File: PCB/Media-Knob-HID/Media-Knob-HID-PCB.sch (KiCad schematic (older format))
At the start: 0 parts

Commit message: Interface und Powersupply
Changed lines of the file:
@@
 $Descr A4 11693 8268
 encoding utf-8
-Sheet 1 5
+Sheet 1 7
 Title "Media-Knob_HID"
-Date "2020-11-08"
+Date "2020-12-13"
 Rev "V0.1"
 Comp "Benedikt Graf"
@@
 $EndDescr
 $Sheet
-S 6400 3400 750  300
+S 7050 3250 750  300
 U 5FAB02B0
 F0 "LED_Ring" 50
 F1 "LED_Ring.sch" 50
-F2 "LED_RING_IN" I L 6400 3500 50
+F2 "LED_RING_IN" I L 7050 3350 50
 $EndSheet
 $Sheet
-S 6400 2150 750  950
+S 7050 2000 750  950
 U 5FAB02CF
 F0 "Input" 50
 F1 "Input.sch" 50
-F2 "Rotary_SW" O L 6400 2200 50
-F3 "Rotary_B" O L 6400 2400 50
-F4 "Rotary_A" O L 6400 2300 50
-F5 "SW1" O L 6400 2600 50
-F6 "SW2" O L 6400 2700 50
-F7 "SW3" O L 6400 2800 50
-F8 "SW4" O L 6400 2900 50
-F9 "SW5" O L 6400 3000 50
+F2 "Rotary_SW" O L 7050 2050 50
+F3 "Rotary_B" O L 7050 2250 50
+F4 "Rotary_A" O L 7050 2150 50
+F5 "SW1" O L 7050 2450 50
+F6 "SW2" O L 7050 2550 50
+F7 "SW3" O L 7050 2650 50
+F8 "SW4" O L 7050 2750 50
+F9 "SW5" O L 7050 2850 50
 $EndSheet
 Wire Wire Line
-	6200 3500 6400 3500
+	6850 3350 7050 3350
 Wire Wire Line
-	6200 3000 6400 3000
+	6850 2850 7050 2850
 Wire Wire Line
-	6200 2900 6400 2900
+	6850 2750 7050 2750
 Wire Wire Line
-	6200 2800 6400 2800
+	6850 2650 7050 2650
 Wire Wire Line
-	6200 2700 6400 2700
+	6850 2550 7050 2550
 Wire Wire Line
-	6200 2600 6400 2600
-Text Notes 7250 2600 0    50   ~ 0
+	6850 2450 7050 2450
+Text Notes 7900 2450 0    50   ~ 0
 Human Input\n
-Text Notes 7250 3550 0    50   ~ 0
+Text Notes 7900 3400 0    50   ~ 0
 Human Output\n
 Wire Wire Line
-	6200 2200 6400 2200
+	6850 2050 7050 2050
 Wire Wire Line
-	6200 2300 6400 2300
+	6850 2150 7050 2150
 Wire Wire Line
-	6200 2400 6400 2400
+	6850 2250 7050 2250
 $Sheet
-S 5100 2150 1100 3150
+S 5750 2000 1100 3150
 U 5FAB027C
 F0 "Microcontroller.sch" 50
 F1 "Microcontroller.sch" 50
-F2 "Rotary_SW" I R 6200 2200 50
-F3 "Rotary_A" I R 6200 2300 50
-F4 "Rotary_B" I R 6200 2400 50
-F5 "LED_RING_IN" O R 6200 3500 50
-F6 "D-" B L 5100 2300 50
-F7 "D+" B L 5100 2200 50
-F8 "RESET" I L 5100 2450 50
-F9 "SW5" I R 6200 3000 50
-F10 "SW4" I R 6200 2900 50
-F11 "SW3" I R 6200 2800 50
-F12 "SW2" I R 6200 2700 50
-F13 "SW1" I R 6200 2600 50
-F14 "Input_Select" O L 5100 2650 39
-F15 "Output_Select" O L 5100 2750 39
+F2 "Rotary_SW" I R 6850 2050 50
+F3 "Rotary_A" I R 6850 2150 50
+F4 "Rotary_B" I R 6850 2250 50
+F5 "LED_RING_IN" O R 6850 3350 50
+F6 "D-" B L 5750 2800 50
+F7 "D+" B L 5750 2700 50
+F8 "RESET" I L 5750 2100 50
+F9 "SW5" I R 6850 2850 50
+F10 "SW4" I R 6850 2750 50
+F11 "SW3" I R 6850 2650 50
+F12 "SW2" I R 6850 2550 50
+F13 "SW1" I R 6850 2450 50
+F14 "Input_Select" O L 5750 2200 39
 $EndSheet
 $Sheet
-S 3750 2150 500  3150
+S 4150 2150 600  2350
 U 5FBD5D88
 F0 "Interface" 50
 F1 "Interface.sch" 50
+F2 "Input_Select" I R 4750 2200 50
+F3 "D-_HOST" B R 4750 2550 50
+F4 "D+_HOST" B R 4750 2450 50
+F5 "D-_Down2" B R 4750 2900 50
+F6 "D+_Down2" B R 4750 2800 50
+F7 "D-_Down3" B R 4750 3200 50
+F8 "D+_Down3" B R 4750 3100 50
+F9 "D-_Down4" B R 4750 3500 50
+F10 "D+_Down4" B R 4750 3400 50
+F11 "D-_Down5" B R 4750 3800 50
+F12 "D+_Down5" B R 4750 3700 50
+F13 "D-_Down6" B R 4750 4100 50
+F14 "D+_Down6" B R 4750 4000 50
+F15 "D-_Down7" B R 4750 4400 50
+F16 "D+_Down7" B R 4750 4300 50
 $EndSheet
+$Sheet
+S 1600 5600 1900 1400
+U 5FDD900C
+F0 "Power_Supply" 50
+F1 "Power_Supply.sch" 50
+$EndSheet
+$Sheet
+S 4900 2350 700  2150
+U 5FDD9032
+F0 "USB_HUB" 50
+F1 "USB_HUB.sch" 50
+$EndSheet
+Wire Wire Line
+	4750 2200 5750 2200
 $EndSCHEMATC

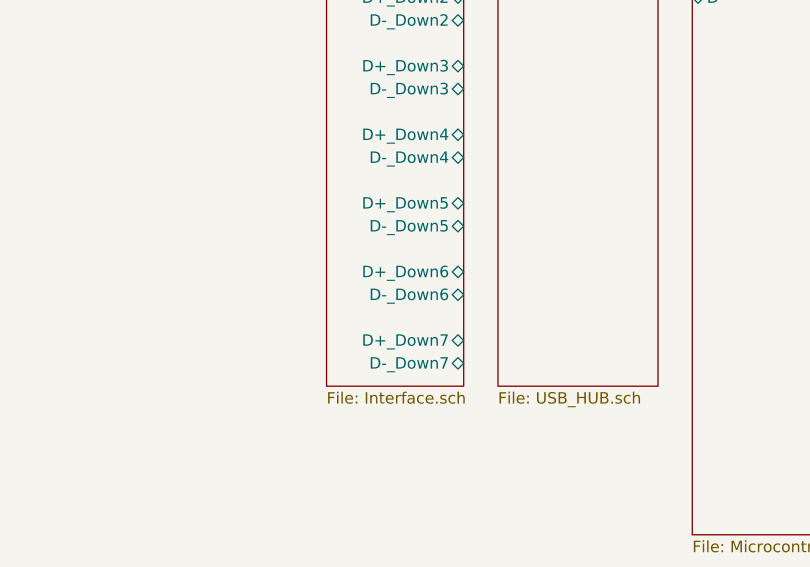
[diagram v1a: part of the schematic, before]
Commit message: ESD Schutz eingefügt und Projekt vereinfacht
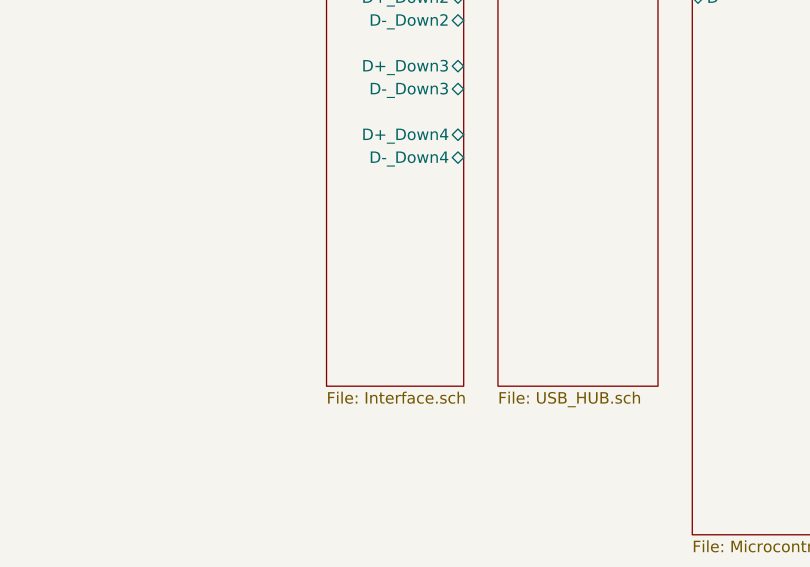
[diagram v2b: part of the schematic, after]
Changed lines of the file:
@@
 F9 "D-_Down4" B R 4750 3500 50
 F10 "D+_Down4" B R 4750 3400 50
-F11 "D-_Down5" B R 4750 3800 50
-F12 "D+_Down5" B R 4750 3700 50
-F13 "D-_Down6" B R 4750 4100 50
-F14 "D+_Down6" B R 4750 4000 50
-F15 "D-_Down7" B R 4750 4400 50
-F16 "D+_Down7" B R 4750 4300 50
 $EndSheet
 $Sheet

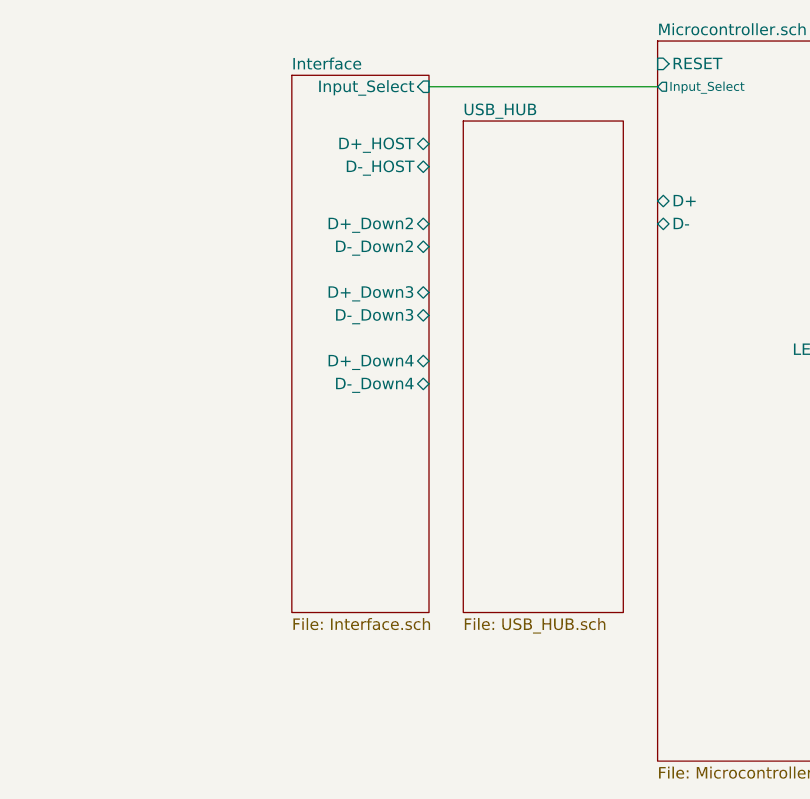
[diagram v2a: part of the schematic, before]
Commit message: Port Switch für USB eingefügt
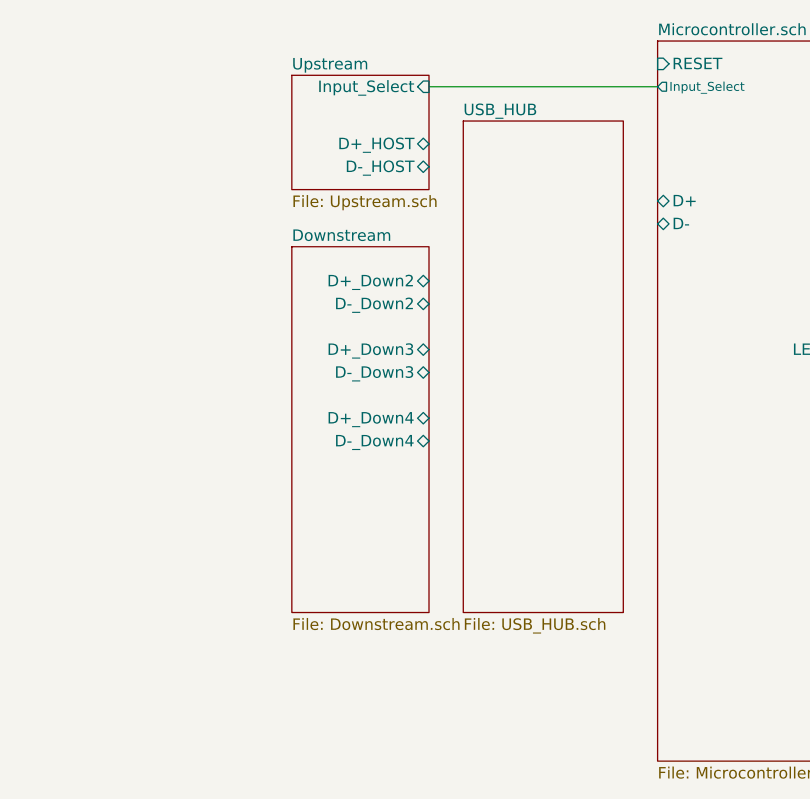
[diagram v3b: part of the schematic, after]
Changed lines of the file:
@@
 $Descr A4 11693 8268
 encoding utf-8
-Sheet 1 7
+Sheet 1 8
 Title "Media-Knob_HID"
 Date "2020-12-13"
@@
 $EndSheet
 $Sheet
-S 4150 2150 600  2350
+S 4150 2150 600  500
 U 5FBD5D88
-F0 "Interface" 50
-F1 "Interface.sch" 50
+F0 "Upstream" 50
+F1 "Upstream.sch" 50
 F2 "Input_Select" I R 4750 2200 50
 F3 "D-_HOST" B R 4750 2550 50
 F4 "D+_HOST" B R 4750 2450 50
-F5 "D-_Down2" B R 4750 2900 50
-F6 "D+_Down2" B R 4750 2800 50
-F7 "D-_Down3" B R 4750 3200 50
-F8 "D+_Down3" B R 4750 3100 50
-F9 "D-_Down4" B R 4750 3500 50
-F10 "D+_Down4" B R 4750 3400 50
 $EndSheet
 $Sheet
@@
 Wire Wire Line
 	4750 2200 5750 2200
+$Sheet
+S 4150 2900 600  1600
+U 602BCB73
+F0 "Downstream" 50
+F1 "Downstream.sch" 50
+F2 "D-_Down4" B R 4750 3750 50
+F3 "D+_Down4" B R 4750 3650 50
+F4 "D-_Down3" B R 4750 3450 50
+F5 "D+_Down3" B R 4750 3350 50
+F6 "D-_Down2" B R 4750 3150 50
+F7 "D+_Down2" B R 4750 3050 50
+$EndSheet
 $EndSCHEMATC

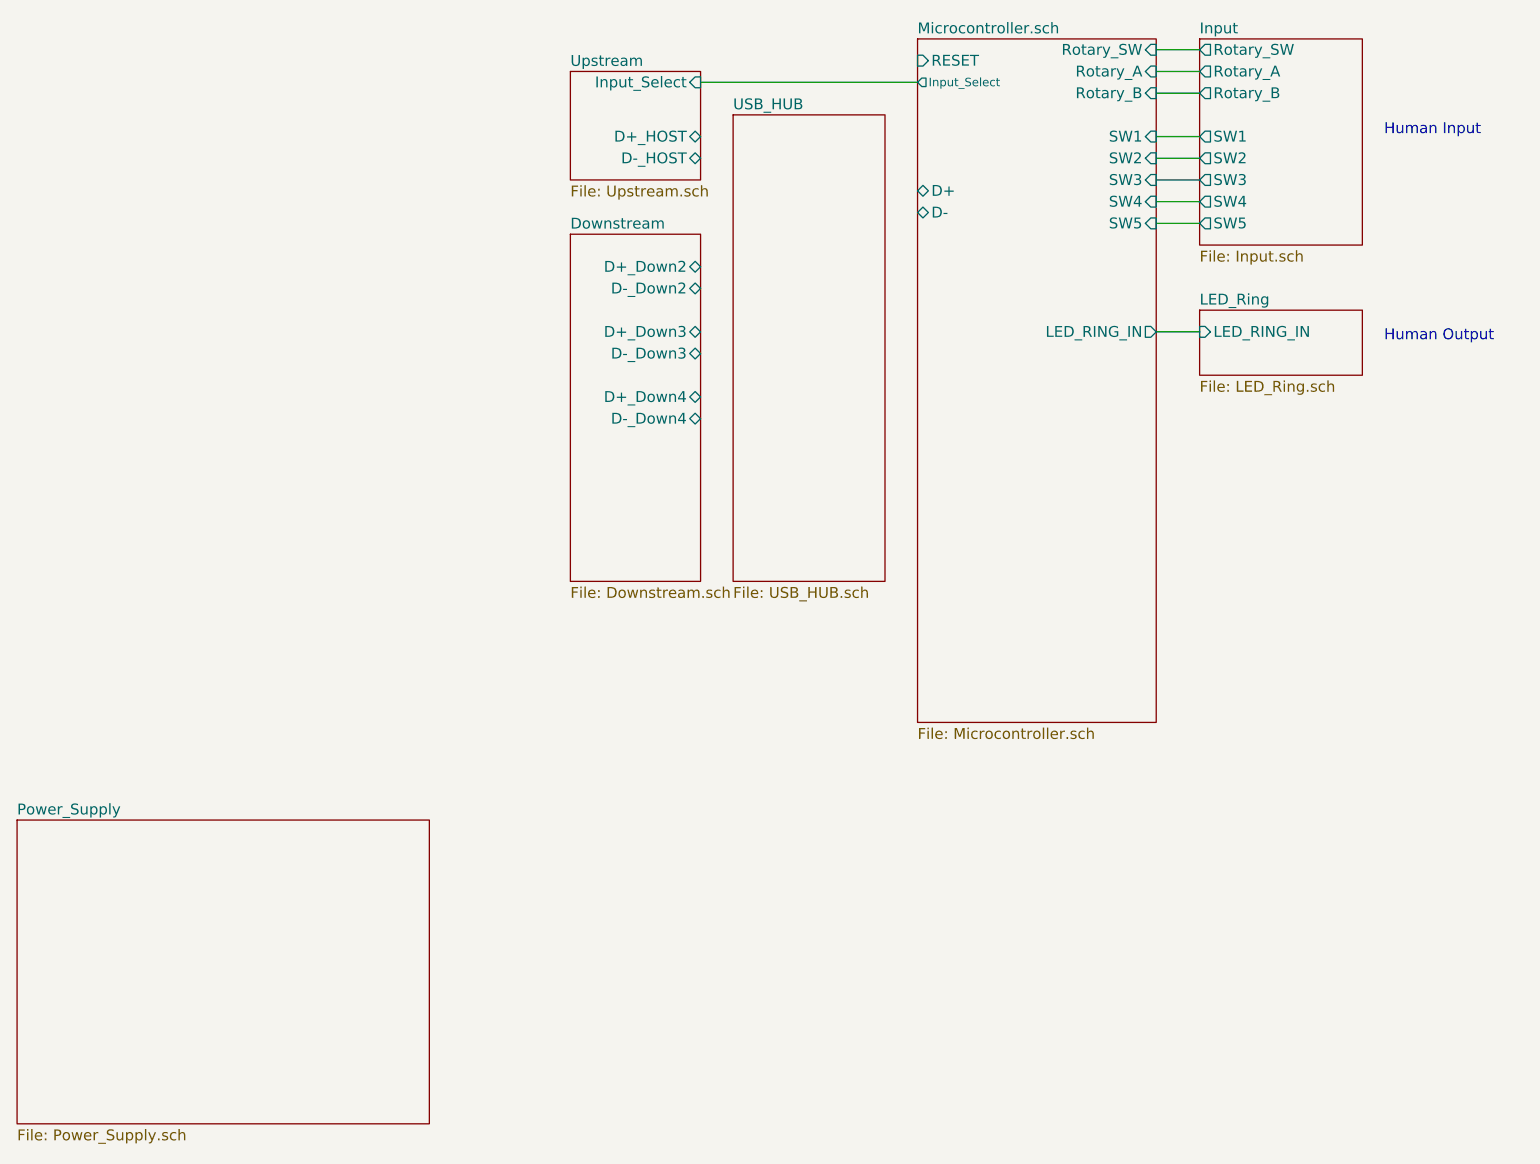
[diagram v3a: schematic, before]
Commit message: Media_knob an neues Konzept angepasst
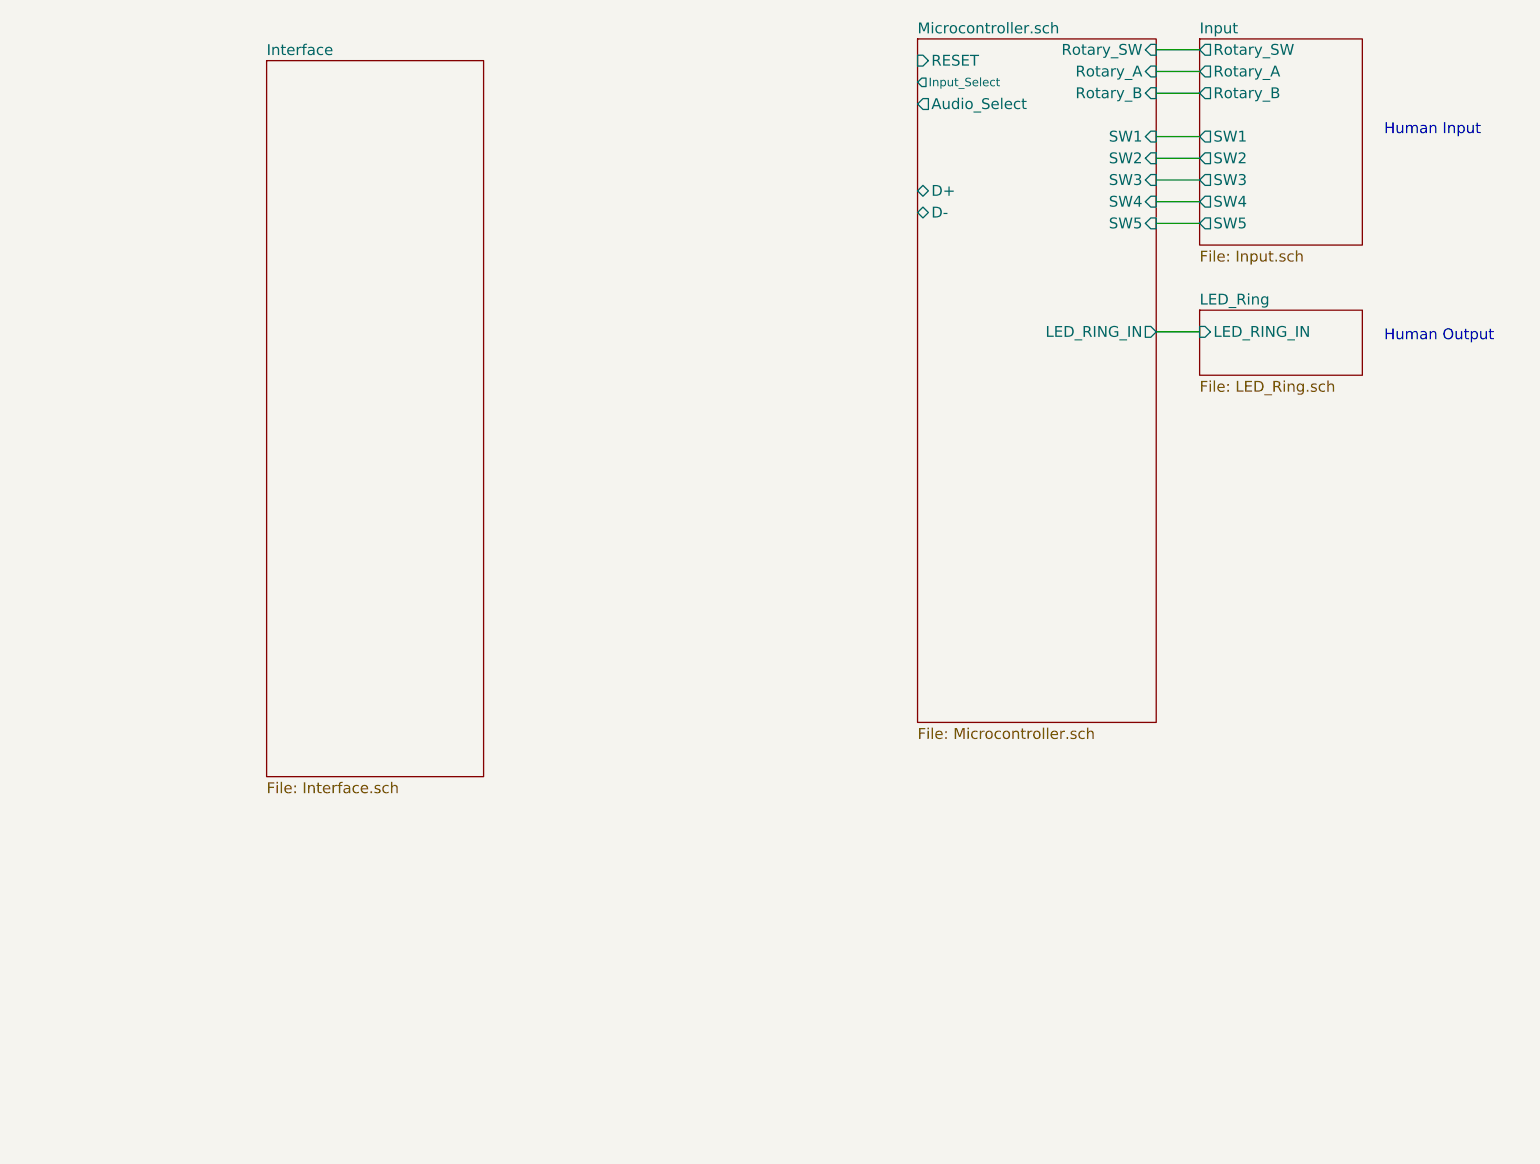
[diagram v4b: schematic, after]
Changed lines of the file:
@@
 $Descr A4 11693 8268
 encoding utf-8
-Sheet 1 8
+Sheet 1 5
 Title "Media-Knob_HID"
 Date "2020-12-13"
@@
 F13 "SW1" I R 6850 2450 50
 F14 "Input_Select" O L 5750 2200 39
+F15 "Audio_Select" O L 5750 2300 50
 $EndSheet
 $Sheet
-S 4150 2150 600  500
-U 5FBD5D88
-F0 "Upstream" 50
-F1 "Upstream.sch" 50
-F2 "Input_Select" I R 4750 2200 50
-F3 "D-_HOST" B R 4750 2550 50
-F4 "D+_HOST" B R 4750 2450 50
-$EndSheet
-$Sheet
-S 1600 5600 1900 1400
-U 5FDD900C
-F0 "Power_Supply" 50
-F1 "Power_Supply.sch" 50
-$EndSheet
-$Sheet
-S 4900 2350 700  2150
-U 5FDD9032
-F0 "USB_HUB" 50
-F1 "USB_HUB.sch" 50
-$EndSheet
-Wire Wire Line
-	4750 2200 5750 2200
-$Sheet
-S 4150 2900 600  1600
-U 602BCB73
-F0 "Downstream" 50
-F1 "Downstream.sch" 50
-F2 "D-_Down4" B R 4750 3750 50
-F3 "D+_Down4" B R 4750 3650 50
-F4 "D-_Down3" B R 4750 3450 50
-F5 "D+_Down3" B R 4750 3350 50
-F6 "D-_Down2" B R 4750 3150 50
-F7 "D+_Down2" B R 4750 3050 50
+S 2750 2100 1000 3300
+U 6090598C
+F0 "Interface" 50
+F1 "Interface.sch" 50
 $EndSheet
 $EndSCHEMATC
